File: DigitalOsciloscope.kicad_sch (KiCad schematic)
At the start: 0 parts

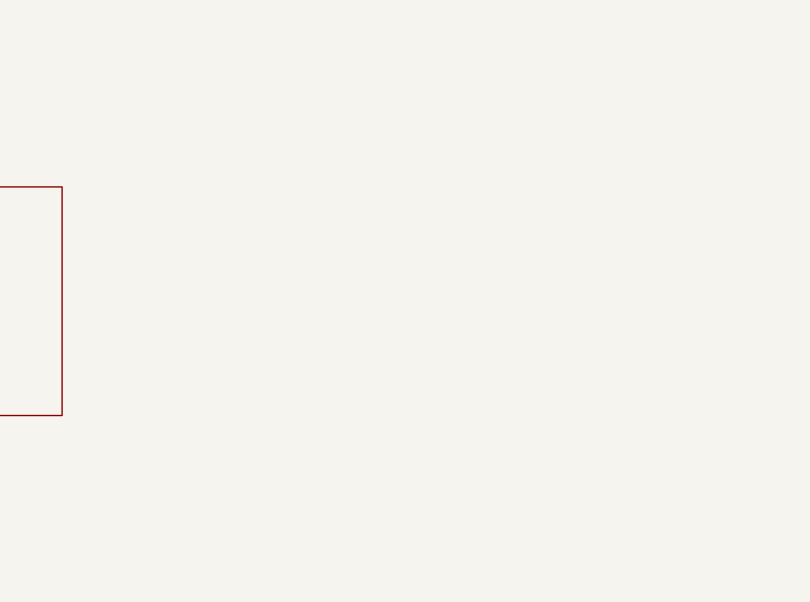
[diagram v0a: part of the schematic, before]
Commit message: Chose amplifiers
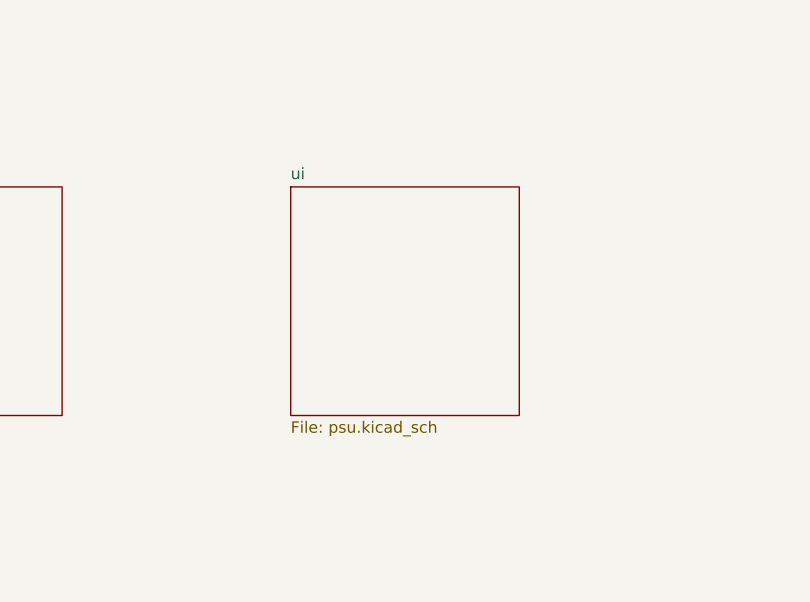
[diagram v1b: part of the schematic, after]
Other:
- added sheet ui (psu.kicad_sch)
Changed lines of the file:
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@@
+		)
+	)
+	(sheet
+		(at 127 76.2)
+		(size 25.4 25.4)
+		(exclude_from_sim no)
+		(in_bom yes)
+		(on_board yes)
+		(dnp no)
+		(fields_autoplaced yes)
+		(stroke
+			(width 0.1524)
+			(type solid)
+		)
+		(fill
+			(color 0 0 0 0.0000)
+		)
+		(property "Sheetname" "ui"
+			(at 127 75.4884 0)
+			(effects
+				(font
+					(size 1.27 1.27)
+				)
+				(justify left bottom)
+			)
+		)
+		(property "Sheetfile" "psu.kicad_sch"
+			(at 127 102.1846 0)
+			(effects
+				(font
+					(size 1.27 1.27)
+				)
+				(justify left top)
+			)
+		)
+		(instances
+			(project "DigitalOsciloscope"
+				(path "/553deb7b-4100-40fe-99d2-0c7b4b56aad2"
+					(page "11")
+				)
+			)
 		)
 	)

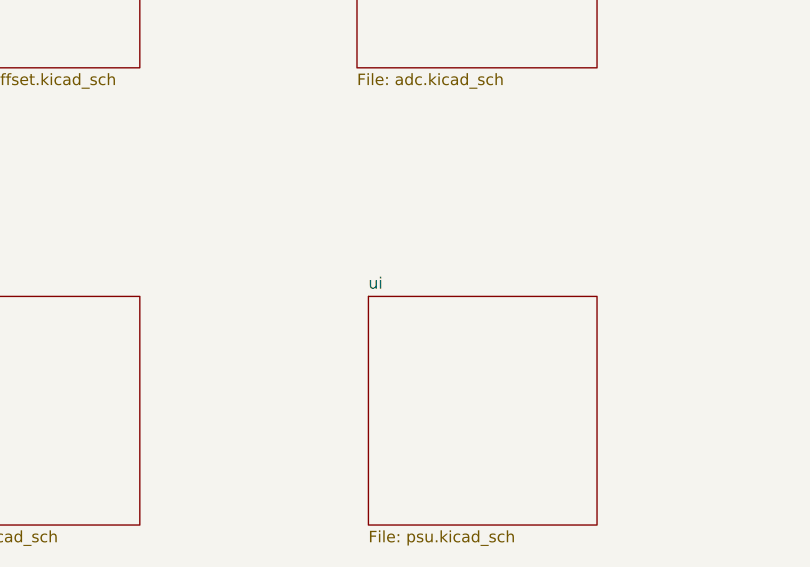
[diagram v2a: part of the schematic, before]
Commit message: First version of analog path, without resistor values
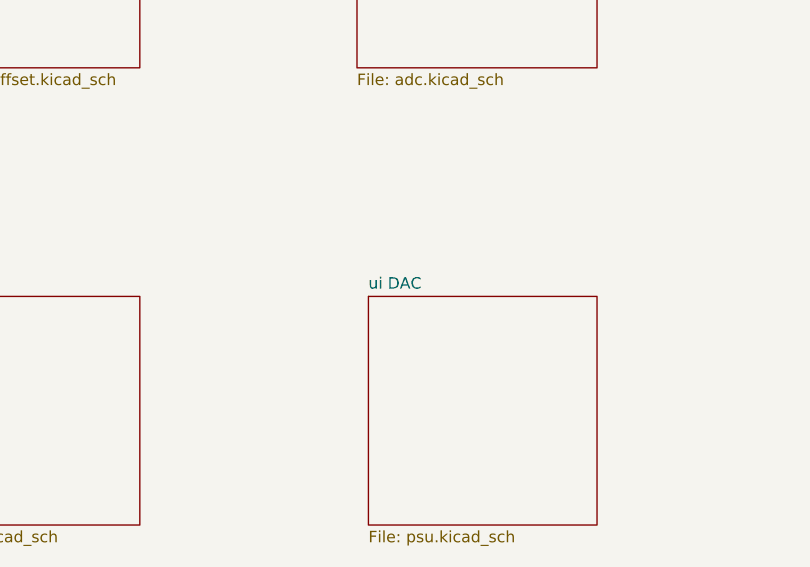
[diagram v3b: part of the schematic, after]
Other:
- sheet ui renamed ui DAC
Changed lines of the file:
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@@
 			(color 0 0 0 0.0000)
 		)
-		(property "Sheetname" "ui"
+		(property "Sheetname" "ui DAC"
 			(at 127 75.4884 0)
 			(effects

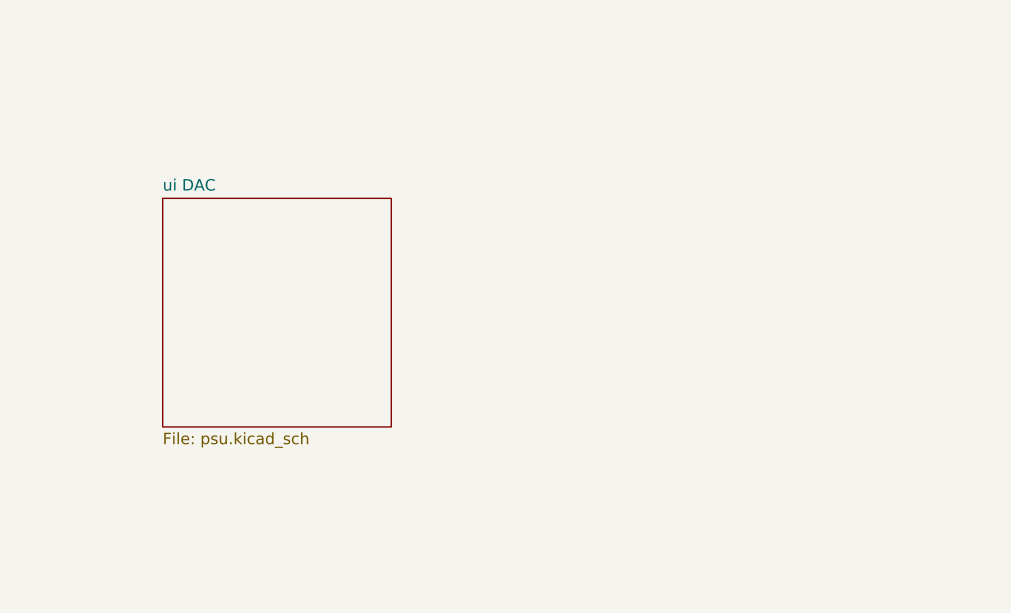
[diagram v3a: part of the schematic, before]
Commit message: Touch up analog front end, add base of the psu
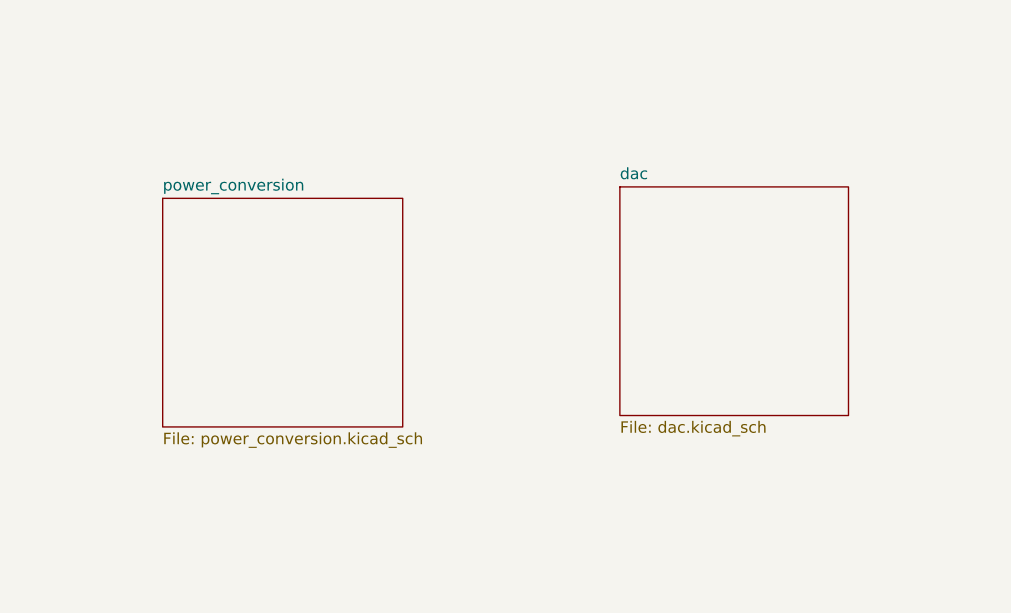
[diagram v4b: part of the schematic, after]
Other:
- removed sheet ui DAC
- added sheet dac (dac.kicad_sch)
- added sheet power_conversion (power_conversion.kicad_sch)
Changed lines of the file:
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@@
+	)
+	(sheet
+		(at 177.8 74.93)
+		(size 25.4 25.4)
+		(exclude_from_sim no)
+		(in_bom yes)
+		(on_board yes)
+		(dnp no)
+		(fields_autoplaced yes)
+		(stroke
+			(width 0.1524)
+			(type solid)
+		)
+		(fill
+			(color 0 0 0 0.0000)
+		)
+		(property "Sheetname" "dac"
+			(at 177.8 74.2184 0)
+			(effects
+				(font
+					(size 1.27 1.27)
+				)
+				(justify left bottom)
+			)
+		)
+		(property "Sheetfile" "dac.kicad_sch"
+			(at 177.8 100.9146 0)
+			(effects
+				(font
+					(size 1.27 1.27)
+				)
+				(justify left top)
+			)
+		)
+		(instances
+			(project "DigitalOsciloscope"
+				(path "/553deb7b-4100-40fe-99d2-0c7b4b56aad2"
+					(page "12")
+				)
+			)
+		)
+	)
+	(sheet
+		(at 127 76.2)
+		(size 26.67 25.4)
+		(exclude_from_sim no)
+		(in_bom yes)
+		(on_board yes)
+		(dnp no)
+		(fields_autoplaced yes)
+		(stroke
+			(width 0.1524)
+			(type solid)
+		)
+		(fill
+			(color 0 0 0 0.0000)
+		)
+		(property "Sheetname" "power_conversion"
+			(at 127 75.4884 0)
+			(effects
+				(font
+					(size 1.27 1.27)
+				)
+				(justify left bottom)
+			)
+		)
+		(property "Sheetfile" "power_conversion.kicad_sch"
+			(at 127 102.1846 0)
+			(effects
+				(font
+					(size 1.27 1.27)
+				)
+				(justify left top)
+			)
+		)
+		(instances
+			(project "DigitalOsciloscope"
+				(path "/553deb7b-4100-40fe-99d2-0c7b4b56aad2"
+					(page "11")
+				)
+			)
+		)
 	)
 	(sheet
@@
 				)
 			)
-		)
-	)
-	(sheet
-		(at 127 76.2)
-		(size 25.4 25.4)
-		(exclude_from_sim no)
-		(in_bom yes)
-		(on_board yes)
-		(dnp no)
-		(fields_autoplaced yes)
-		(stroke
-			(width 0.1524)
-			(type solid)
-		)
-		(fill
-			(color 0 0 0 0.0000)
-		)
-		(property "Sheetname" "ui DAC"
-			(at 127 75.4884 0)
-			(effects
-				(font
-					(size 1.27 1.27)
-				)
-				(justify left bottom)
-			)
-		)
-		(property "Sheetfile" "psu.kicad_sch"
-			(at 127 102.1846 0)
-			(effects
-				(font
-					(size 1.27 1.27)
-				)
-				(justify left top)
-			)
-		)
-		(instances
-			(project "DigitalOsciloscope"
-				(path "/553deb7b-4100-40fe-99d2-0c7b4b56aad2"
-					(page "11")
-				)
-			)

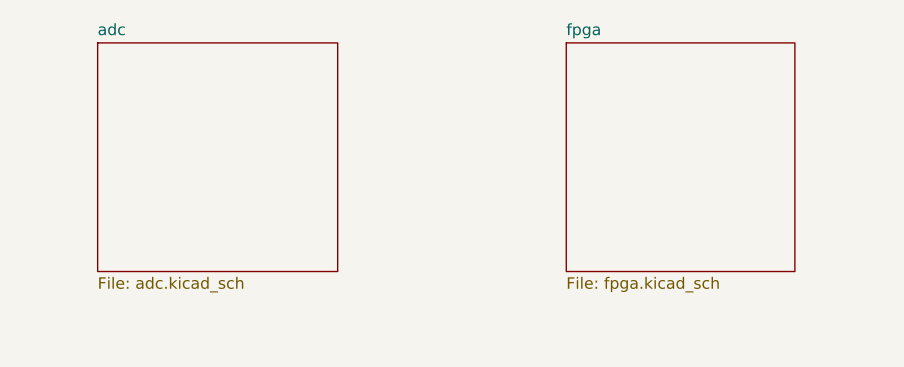
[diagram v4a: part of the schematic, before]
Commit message: Link up ADC to FPGA
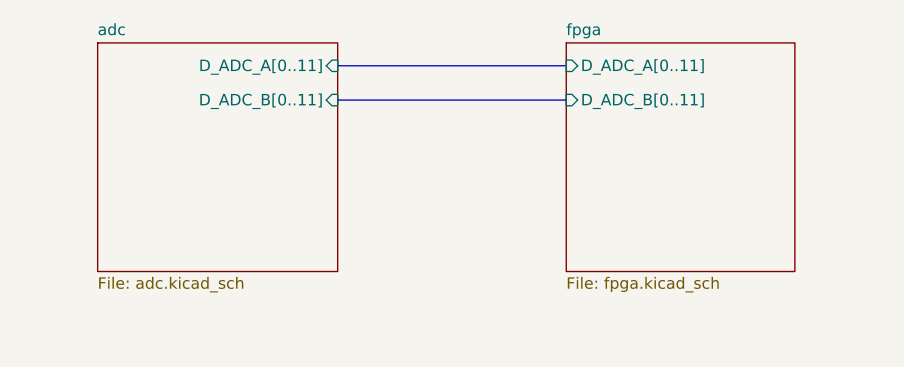
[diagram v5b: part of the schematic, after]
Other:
- sheet adc ports: added D_ADC_A[0..11], D_ADC_B[0..11]; removed none
- sheet fpga ports: added D_ADC_A[0..11], D_ADC_B[0..11]; removed none
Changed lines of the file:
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@@
+		)
+	)
+	(bus
+		(pts
+			(xy 152.4 31.75) (xy 177.8 31.75)
+		)
+		(stroke
+			(width 0)
+			(type default)
+		)
+	)
+	(bus
+		(pts
+			(xy 152.4 27.94) (xy 177.8 27.94)
+		)
+		(stroke
+			(width 0)
+			(type default)
 		)
 	)
@@
 			)
 		)
+		(pin "D_ADC_A[0..11]" input
+			(at 177.8 27.94 180)
+			(effects
+				(font
+					(size 1.27 1.27)
+				)
+				(justify left)
+			)
+		)
+		(pin "D_ADC_B[0..11]" input
+			(at 177.8 31.75 180)
+			(effects
+				(font
+					(size 1.27 1.27)
+				)
+				(justify left)
+			)
+		)
 		(instances
 			(project "DigitalOsciloscope"
@@
 			)
 		)
+		(pin "D_ADC_A[0..11]" input
+			(at 152.4 27.94 0)
+			(effects
+				(font
+					(size 1.27 1.27)
+				)
+				(justify right)
+			)
+		)
+		(pin "D_ADC_B[0..11]" input
+			(at 152.4 31.75 0)
+			(effects
+				(font
+					(size 1.27 1.27)
+				)
+				(justify right)
+			)
+		)

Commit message: Add things to MCU on the board
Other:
- removed sheet external_flash
- removed sheet external_ram
- note removed: "Optional"
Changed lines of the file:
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@@
 	(generator_version "9.0")
 	(paper "A4")
-	(rectangle
-		(start 22.86 137.16)
-		(end 124.46 187.96)
-		(stroke
-			(width 0)
-			(type default)
-		)
-		(fill
-			(type none)
-		)
-	)
-	(text "Optional"
-		(exclude_from_sim no)
-		(at 28.702 134.366 0)
-		(effects
-			(font
-				(size 1.27 1.27)
-			)
-		)
-	)
 	(bus
 		(pts
@@
 	)
 	(sheet
-		(at 78.74 152.4)
-		(size 33.02 22.86)
-		(exclude_from_sim no)
-		(in_bom yes)
-		(on_board yes)
-		(dnp no)
-		(fields_autoplaced yes)
-		(stroke
-			(width 0.1524)
-			(type solid)
-		)
-		(fill
-			(color 0 0 0 0.0000)
-		)
-		(property "Sheetname" "external_flash"
-			(at 78.74 151.6884 0)
-			(effects
-				(font
-					(size 1.27 1.27)
-				)
-				(justify left bottom)
-			)
-		)
-		(property "Sheetfile" "external_flash.kicad_sch"
-			(at 78.74 175.8446 0)
-			(effects
-				(font
-					(size 1.27 1.27)
-				)
-				(justify left top)
-			)
-		)
-		(instances
-			(project "DigitalOsciloscope"
-				(path "/553deb7b-4100-40fe-99d2-0c7b4b56aad2"
-					(page "7")
-				)
-			)
-		)
-	)
-	(sheet
 		(at 177.8 25.4)
 		(size 25.4 25.4)
@@
 				)
 			)
-		)
-	)
-	(sheet
-		(at 35.56 151.13)
-		(size 31.75 25.4)
-		(exclude_from_sim no)
-		(in_bom yes)
-		(on_board yes)
-		(dnp no)
-		(fields_autoplaced yes)
-		(stroke
-			(width 0.1524)
-			(type solid)
-		)
-		(fill
-			(color 0 0 0 0.0000)
-		)
-		(property "Sheetname" "external_ram"
-			(at 35.56 150.4184 0)
-			(effects
-				(font
-					(size 1.27 1.27)
-				)
-				(justify left bottom)
-			)
-		)
-		(property "Sheetfile" "external_ram.kicad_sch"
-			(at 35.56 177.1146 0)
-			(effects
-				(font
-					(size 1.27 1.27)
-				)
-				(justify left top)
-			)
-		)
-		(instances
-			(project "DigitalOsciloscope"
-				(path "/553deb7b-4100-40fe-99d2-0c7b4b56aad2"
-					(page "6")
-				)
-			)
